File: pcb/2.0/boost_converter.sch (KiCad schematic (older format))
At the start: 11 parts

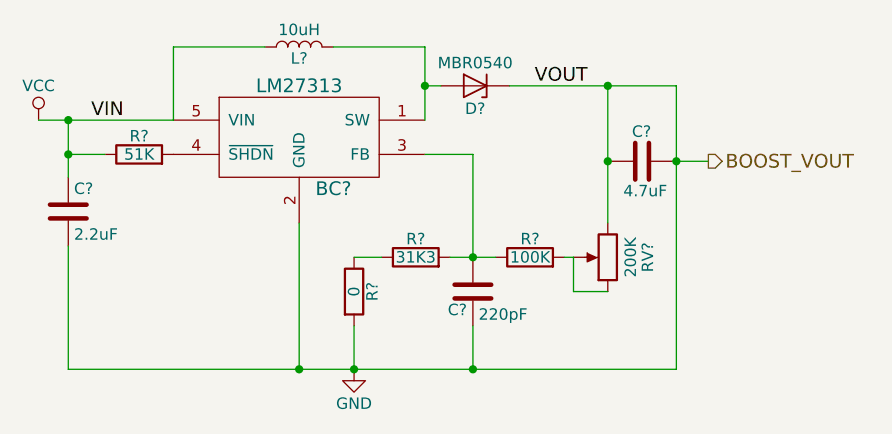
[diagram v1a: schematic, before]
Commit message: add the sound circuit
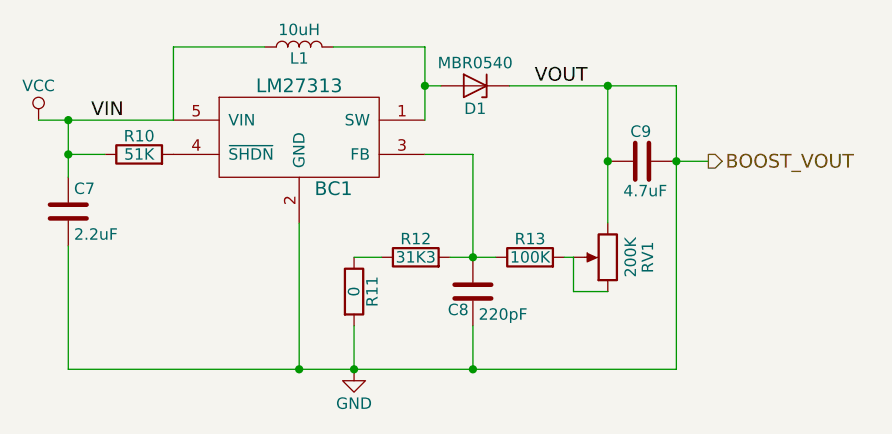
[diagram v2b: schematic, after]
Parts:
- gave numbers to parts that had none: 11
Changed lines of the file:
@@
 $EndDescr
 $Comp
-L L L?
+L L L1
 U 1 1 5A30CDF1
 P 5480 2990
-F 0 "L?" V 5430 2990 50  0000 C CNN
+F 0 "L1" V 5430 2990 50  0000 C CNN
 F 1 "10uH" V 5555 2990 50  0000 C CNN
 F 2 "components:Inductor_PIS2408_SMD" H 5480 2990 50  0001 C CNN
@@
 $EndComp
 $Comp
-L D_Zener D?
+L D_Zener D1
 U 1 1 5A30CDF2
 P 6250 3160
-F 0 "D?" H 6250 3260 50  0000 C CNN
+F 0 "D1" H 6250 3260 50  0000 C CNN
 F 1 "MBR0540" H 6250 3060 50  0000 C CNN
 F 2 "Diodes_SMD:D_SOD-323_HandSoldering" H 6250 3160 50  0001 C CNN
@@
 $EndComp
 $Comp
-L R R?
+L R R13
 U 1 1 5A30CDF3
 P 6490 3910
-F 0 "R?" V 6570 3910 50  0000 C CNN
+F 0 "R13" V 6570 3910 50  0000 C CNN
 F 1 "100K" V 6490 3910 50  0000 C CNN
 F 2 "Resistors_SMD:R_1206_HandSoldering" V 6420 3910 50  0001 C CNN
@@
 $EndComp
 $Comp
-L C C?
+L C C8
 U 1 1 5A30CDF4
 P 6240 4060
-F 0 "C?" H 6130 3980 50  0000 L CNN
+F 0 "C8" H 6130 3980 50  0000 L CNN
 F 1 "220pF" H 6265 3960 50  0000 L CNN
 F 2 "Capacitors_SMD:C_1206_HandSoldering" H 6278 3910 50  0001 C CNN
@@
 $EndComp
 $Comp
-L R R?
+L R R12
 U 1 1 5A30CDF5
 P 5990 3910
-F 0 "R?" V 6070 3910 50  0000 C CNN
+F 0 "R12" V 6070 3910 50  0000 C CNN
 F 1 "31K3" V 5990 3910 50  0000 C CNN
 F 2 "Resistors_SMD:R_1206_HandSoldering" V 5920 3910 50  0001 C CNN
@@
 $EndComp
 $Comp
-L R R?
+L R R10
 U 1 1 5A30CDF6
 P 4780 3460
-F 0 "R?" V 4860 3460 50  0000 C CNN
+F 0 "R10" V 4860 3460 50  0000 C CNN
 F 1 "51K" V 4780 3460 50  0000 C CNN
 F 2 "Resistors_SMD:R_1206_HandSoldering" V 4710 3460 50  0001 C CNN
@@
 $EndComp
 $Comp
-L LM27313 BC?
+L LM27313 BC1
 U 1 1 5A30CDF7
 P 5480 3410
-F 0 "BC?" H 5630 3210 60  0000 C CNN
+F 0 "BC1" H 5630 3210 60  0000 C CNN
 F 1 "LM27313" H 5480 3660 60  0000 C CNN
 F 2 "TO_SOT_Packages_SMD:SOT-23-5_HandSoldering" H 5580 3360 60  0001 C CNN
@@
 $EndComp
 $Comp
-L C C?
+L C C7
 U 1 1 5A30CDF8
 P 4470 3710
-F 0 "C?" H 4495 3810 50  0000 L CNN
+F 0 "C7" H 4495 3810 50  0000 L CNN
 F 1 "2.2uF" H 4495 3610 50  0000 L CNN
 F 2 "Capacitors_SMD:C_1206_HandSoldering" H 4508 3560 50  0001 C CNN
@@
 VOUT
 $Comp
-L POT RV?
+L POT RV1
 U 1 1 5A30CDFB
 P 6830 3910
-F 0 "RV?" V 6655 3910 50  0000 C CNN
+F 0 "RV1" V 6655 3910 50  0000 C CNN
 F 1 "200K" V 6730 3910 50  0000 C CNN
 F 2 "Potentiometers:Potentiometer_Trimmer_Vishay_T73XW_Vertical" H 6830 3910 50  0001 C CNN
@@
 $EndComp
 $Comp
-L C C?
+L C C9
 U 1 1 5A30CDFC
 P 6980 3490
-F 0 "C?" V 7110 3450 50  0000 L CNN
+F 0 "C9" V 7110 3450 50  0000 L CNN
 F 1 "4.7uF" V 6850 3380 50  0000 L CNN
 F 2 "Capacitors_SMD:C_1206_HandSoldering" H 7018 3340 50  0001 C CNN
@@
 $EndComp
 $Comp
-L R R?
+L R R11
 U 1 1 5A30CDFD
 P 5720 4060
-F 0 "R?" V 5800 4060 50  0000 C CNN
+F 0 "R11" V 5800 4060 50  0000 C CNN
 F 1 "0" V 5720 4060 50  0000 C CNN
 F 2 "Resistors_SMD:R_1206_HandSoldering" V 5650 4060 50  0001 C CNN
@@
 	7270 3490 7130 3490
 $Comp
-L VCC #PWR?
+L VCC #PWR40
 U 1 1 5A30F671
 P 4340 3310
-F 0 "#PWR?" H 4340 3160 50  0001 C CNN
+F 0 "#PWR40" H 4340 3160 50  0001 C CNN
 F 1 "VCC" H 4340 3460 50  0000 C CNN
 F 2 "" H 4340 3310 50  0001 C CNN
@@
 Connection ~ 6240 4400
 $Comp
-L GND #PWR?
+L GND #PWR41
 U 1 1 5A30FE4F
 P 5720 4400
-F 0 "#PWR?" H 5720 4150 50  0001 C CNN
+F 0 "#PWR41" H 5720 4150 50  0001 C CNN
 F 1 "GND" H 5720 4250 50  0000 C CNN
 F 2 "" H 5720 4400 50  0001 C CNN

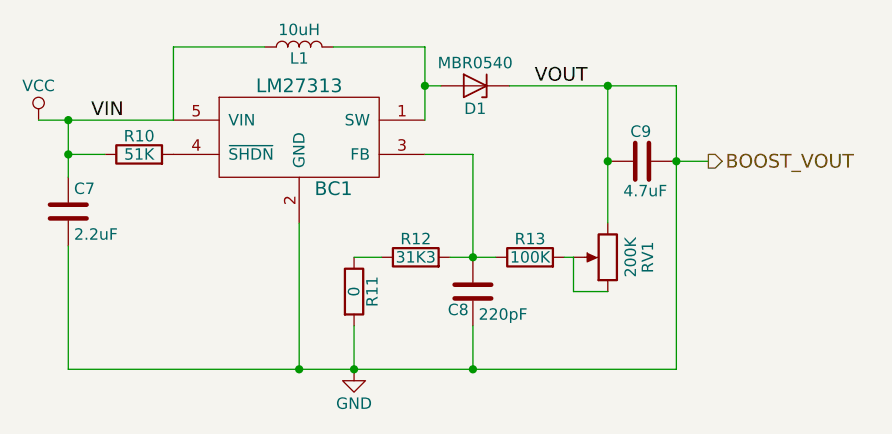
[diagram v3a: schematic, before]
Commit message: complete the 2.0 schematic
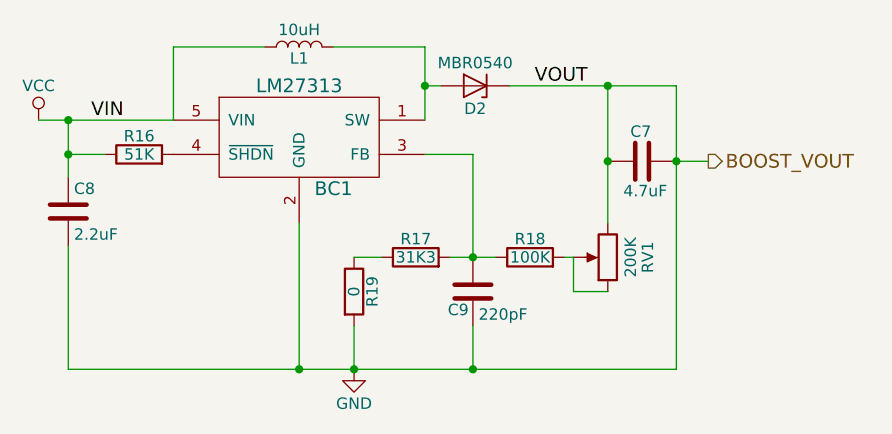
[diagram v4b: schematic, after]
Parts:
- renumbered C9 to C7, C7 to C8, C8 to C9, D1 to D2, R10 to R16, R12 to R17, R13 to R18, R11 to R19
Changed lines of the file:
@@
 $EndComp
 $Comp
-L D_Zener D1
+L D_Zener D2
 U 1 1 5A30CDF2
 P 6250 3160
-F 0 "D1" H 6250 3260 50  0000 C CNN
+F 0 "D2" H 6250 3260 50  0000 C CNN
 F 1 "MBR0540" H 6250 3060 50  0000 C CNN
 F 2 "Diodes_SMD:D_SOD-323_HandSoldering" H 6250 3160 50  0001 C CNN
@@
 $EndComp
 $Comp
-L R R13
+L R R18
 U 1 1 5A30CDF3
 P 6490 3910
-F 0 "R13" V 6570 3910 50  0000 C CNN
+F 0 "R18" V 6570 3910 50  0000 C CNN
 F 1 "100K" V 6490 3910 50  0000 C CNN
 F 2 "Resistors_SMD:R_1206_HandSoldering" V 6420 3910 50  0001 C CNN
@@
 $EndComp
 $Comp
-L C C8
+L C C9
 U 1 1 5A30CDF4
 P 6240 4060
-F 0 "C8" H 6130 3980 50  0000 L CNN
+F 0 "C9" H 6130 3980 50  0000 L CNN
 F 1 "220pF" H 6265 3960 50  0000 L CNN
 F 2 "Capacitors_SMD:C_1206_HandSoldering" H 6278 3910 50  0001 C CNN
@@
 $EndComp
 $Comp
-L R R12
+L R R17
 U 1 1 5A30CDF5
 P 5990 3910
-F 0 "R12" V 6070 3910 50  0000 C CNN
+F 0 "R17" V 6070 3910 50  0000 C CNN
 F 1 "31K3" V 5990 3910 50  0000 C CNN
 F 2 "Resistors_SMD:R_1206_HandSoldering" V 5920 3910 50  0001 C CNN
@@
 $EndComp
 $Comp
-L R R10
+L R R16
 U 1 1 5A30CDF6
 P 4780 3460
-F 0 "R10" V 4860 3460 50  0000 C CNN
+F 0 "R16" V 4860 3460 50  0000 C CNN
 F 1 "51K" V 4780 3460 50  0000 C CNN
 F 2 "Resistors_SMD:R_1206_HandSoldering" V 4710 3460 50  0001 C CNN
@@
 $EndComp
 $Comp
-L C C7
+L C C8
 U 1 1 5A30CDF8
 P 4470 3710
-F 0 "C7" H 4495 3810 50  0000 L CNN
+F 0 "C8" H 4495 3810 50  0000 L CNN
 F 1 "2.2uF" H 4495 3610 50  0000 L CNN
 F 2 "Capacitors_SMD:C_1206_HandSoldering" H 4508 3560 50  0001 C CNN
@@
 $EndComp
 $Comp
-L C C9
+L C C7
 U 1 1 5A30CDFC
 P 6980 3490
-F 0 "C9" V 7110 3450 50  0000 L CNN
+F 0 "C7" V 7110 3450 50  0000 L CNN
 F 1 "4.7uF" V 6850 3380 50  0000 L CNN
 F 2 "Capacitors_SMD:C_1206_HandSoldering" H 7018 3340 50  0001 C CNN
@@
 $EndComp
 $Comp
-L R R11
+L R R19
 U 1 1 5A30CDFD
 P 5720 4060
-F 0 "R11" V 5800 4060 50  0000 C CNN
+F 0 "R19" V 5800 4060 50  0000 C CNN
 F 1 "0" V 5720 4060 50  0000 C CNN
 F 2 "Resistors_SMD:R_1206_HandSoldering" V 5650 4060 50  0001 C CNN
@@
 Connection ~ 6830 3490
 Wire Wire Line
-	7130 4400 7130 3160
+	7130 3160 7130 4400
 Connection ~ 7130 3490
 Wire Wire Line
 	7270 3490 7130 3490
 $Comp
-L VCC #PWR40
+L VCC #PWR040
 U 1 1 5A30F671
 P 4340 3310
-F 0 "#PWR40" H 4340 3160 50  0001 C CNN
+F 0 "#PWR040" H 4340 3160 50  0001 C CNN
 F 1 "VCC" H 4340 3460 50  0000 C CNN
 F 2 "" H 4340 3310 50  0001 C CNN
@@
 $EndComp
 Wire Wire Line
-	4470 4400 7130 4400
+	7130 4400 4470 4400
 Connection ~ 5480 4400
 Connection ~ 5720 4400
 Connection ~ 6240 4400
 $Comp
-L GND #PWR41
+L GND #PWR041
 U 1 1 5A30FE4F
 P 5720 4400
-F 0 "#PWR41" H 5720 4150 50  0001 C CNN
+F 0 "#PWR041" H 5720 4150 50  0001 C CNN
 F 1 "GND" H 5720 4250 50  0000 C CNN
 F 2 "" H 5720 4400 50  0001 C CNN

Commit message: start mapping components to footprints
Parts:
- RV1: footprint Potentiometers:Potentiometer_Trimmer_Vishay_T73XW_Vertical -> Potentiometers:Potentiometer_Trimmer_Bourns_3339P_Horizontal
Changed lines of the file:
@@
 F 0 "RV1" V 6655 3910 50  0000 C CNN
 F 1 "200K" V 6730 3910 50  0000 C CNN
-F 2 "Potentiometers:Potentiometer_Trimmer_Vishay_T73XW_Vertical" H 6830 3910 50  0001 C CNN
+F 2 "Potentiometers:Potentiometer_Trimmer_Bourns_3339P_Horizontal" H 6830 3910 50  0001 C CNN
 F 3 "" H 6830 3910 50  0001 C CNN
 	1    6830 3910
@@
 	7270 3490 7130 3490
 $Comp
-L VCC #PWR53
+L VCC #PWR053
 U 1 1 5A30F671
 P 4340 3310
-F 0 "#PWR53" H 4340 3160 50  0001 C CNN
+F 0 "#PWR053" H 4340 3160 50  0001 C CNN
 F 1 "VCC" H 4340 3460 50  0000 C CNN
 F 2 "" H 4340 3310 50  0001 C CNN
@@
 Connection ~ 6240 4400
 $Comp
-L GND #PWR54
+L GND #PWR054
 U 1 1 5A30FE4F
 P 5720 4400
-F 0 "#PWR54" H 5720 4150 50  0001 C CNN
+F 0 "#PWR054" H 5720 4150 50  0001 C CNN
 F 1 "GND" H 5720 4250 50  0000 C CNN
 F 2 "" H 5720 4400 50  0001 C CNN
